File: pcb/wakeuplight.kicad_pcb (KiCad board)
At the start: 2 copper layers, 129 x 85 mm, 50 parts, among them J1 691322310002, J10 MKDS 3.5mm, J2 Conn_01x19, J3 Conn_01x19, J4 MAX98357A Breakout, J5 MKDS 3.5mm, J6 MKDS 3.5mm, J7 MPT 2,54, J8 MPT 2,54, J9 MKDS 3.5mm, Q1 PSMN1R2-30YLC, Q2 PSMN1R2-30YLC, Q3 T2N7002BK, U1 MCP14A0302, U2 MCP14A0302, U3 LMR16006YQ

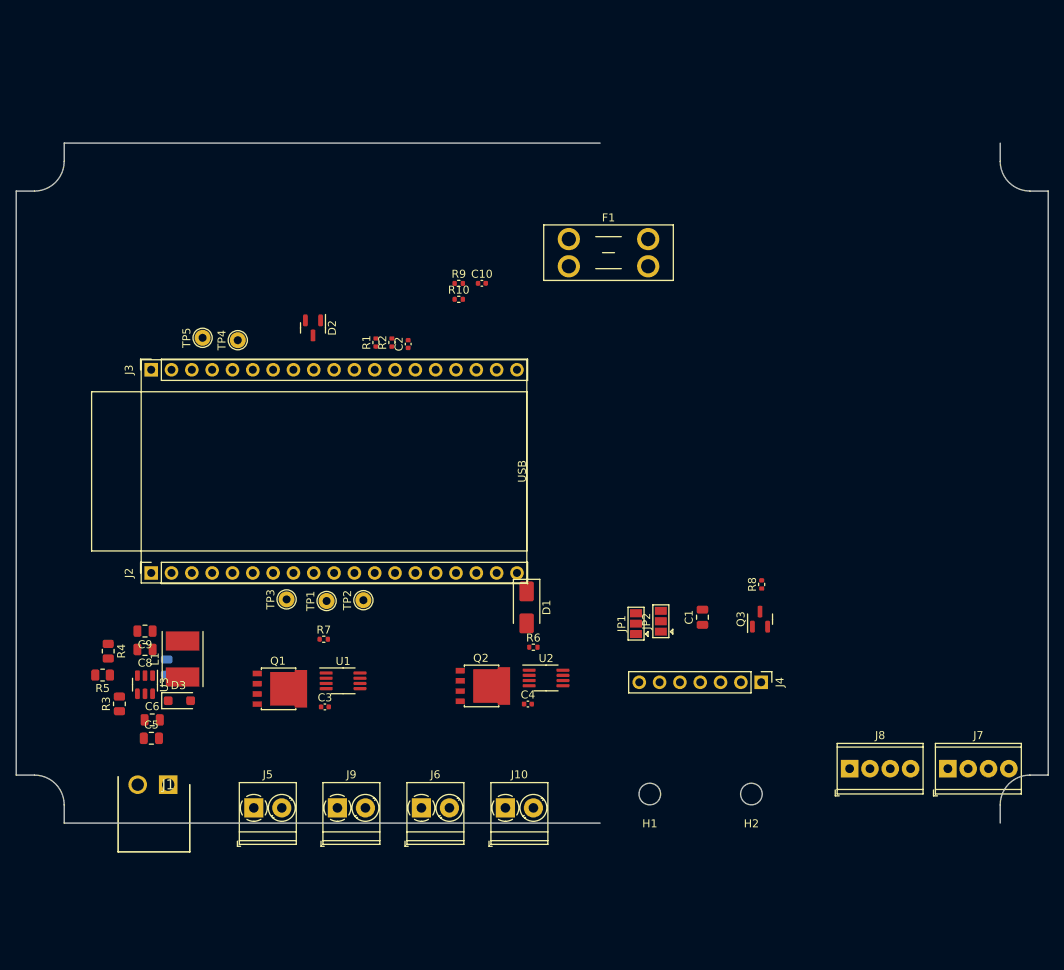
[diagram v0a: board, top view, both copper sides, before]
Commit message: work on PCB: line out + power done ; removed amplifier from board
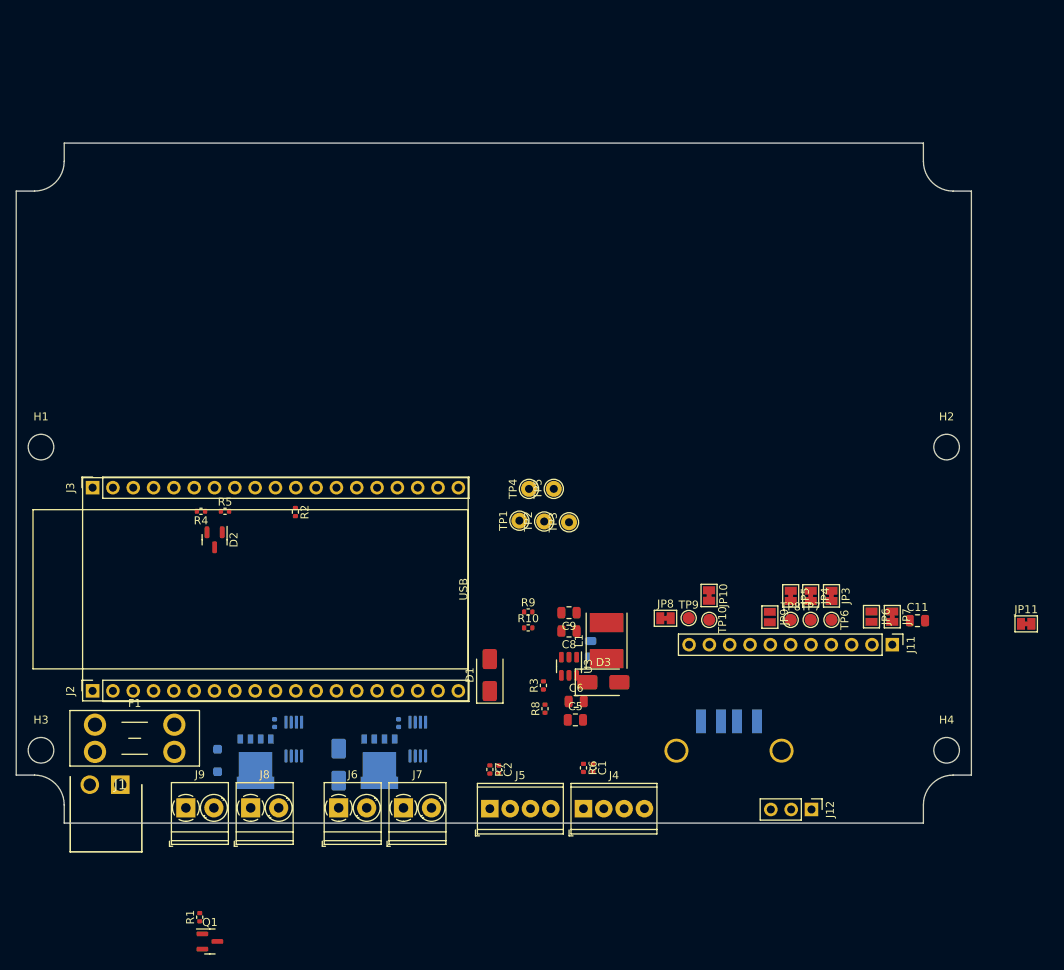
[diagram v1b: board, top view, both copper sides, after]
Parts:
- removed C10: 1uF 10V, Capacitor_SMD:C_0402_1005Metric
- removed J10: MKDS 3.5mm, TerminalBlock_Phoenix:TerminalBlock_Phoenix_PT-1,5-2-3.5-H_1x02_P3.50mm_Horizontal
- removed JP1, JP2: SolderJumper_3_Open, Jumper:SolderJumper-3_P1.3mm_Open_Pad1.0x1.5mm
- added C11: 10uF 10V, Capacitor_SMD:C_0805_2012Metric, F.Cu at (112.7, 59.7)
- added D4: SS16_R2_00001 1A, 42V, Diode_SMD:D_SMA, B.Cu at (40.3, 77.7)
- added D5: PMEG2020EH, Diode_SMD:D_SOD-123F, B.Cu at (25.2, 77.2)
- added H3: MountingHole, MountingHole:MountingHole_3.2mm_M3_DIN965, F.Cu at (3.10, 75.9)
- added H4: MountingHole, MountingHole:MountingHole_3.2mm_M3_DIN965, F.Cu at (116.3, 75.9)
- added J11: PCM5102A Breakout, Connector_PinHeader_2.54mm:PinHeader_1x11_P2.54mm_Vertical, F.Cu at (109.5, 62.7)
- added J12: Conn_01x03_Pin, Connector_PinHeader_2.54mm:PinHeader_1x03_P2.54mm_Vertical, F.Cu at (99.4, 83.3)
- added J13: USB_A, Connector_USB:USB_A_TE_292303-7_Horizontal, B.Cu at (89.1, 78.7)
- added JP10: SolderJumper_2_Bridged, Jumper:SolderJumper-2_P1.3mm_Bridged_Pad1.0x1.5mm, F.Cu at (86.6, 56.5)
- added JP11: SolderJumper_2_Bridged, Jumper:SolderJumper-2_P1.3mm_Bridged_Pad1.0x1.5mm, F.Cu at (126.2, 60.1)
- added JP3: SolderJumper_2_Bridged, Jumper:SolderJumper-2_P1.3mm_Bridged_Pad1.0x1.5mm, F.Cu at (101.9, 56.6)
- added JP4: SolderJumper_2_Bridged, Jumper:SolderJumper-2_P1.3mm_Bridged_Pad1.0x1.5mm, F.Cu at (99.3, 56.6)
- added JP5: SolderJumper_2_Bridged, Jumper:SolderJumper-2_P1.3mm_Bridged_Pad1.0x1.5mm, F.Cu at (96.8, 56.6)
- added JP6: SolderJumper_2_Open, Jumper:SolderJumper-2_P1.3mm_Open_Pad1.0x1.5mm, F.Cu at (106.9, 59.2)
- added JP7: SolderJumper_2_Bridged, Jumper:SolderJumper-2_P1.3mm_Bridged_Pad1.0x1.5mm, F.Cu at (109.5, 59.2)
- added JP8: SolderJumper_2_Bridged, Jumper:SolderJumper-2_P1.3mm_Bridged_Pad1.0x1.5mm, F.Cu at (81.2, 59.4)
- added JP9: SolderJumper_2_Open, Jumper:SolderJumper-2_P1.3mm_Open_Pad1.0x1.5mm, F.Cu at (94.2, 59.2)
- added TP10: TestPoint, TestPoint:TestPoint_Pad_D1.5mm, F.Cu at (86.6, 59.6)
- added TP6: TestPoint, TestPoint:TestPoint_Pad_D1.5mm, F.Cu at (101.9, 59.6)
- added TP7: TestPoint, TestPoint:TestPoint_Pad_D1.5mm, F.Cu at (99.3, 59.6)
- added TP8: TestPoint, TestPoint:TestPoint_Pad_D1.5mm, F.Cu at (96.8, 59.6)
- added TP9: TestPoint, TestPoint:TestPoint_Pad_D1.5mm, F.Cu at (84.1, 59.4)
- C1: value 10uF 10V -> 1uF 10V; footprint Capacitor_SMD:C_0805_2012Metric -> Capacitor_SMD:C_0402_1005Metric
- C3, C4, Q2, U1, U2: moved to B.Cu
- D3: value PMEG2020EH -> SS16_R2_00001 1A, 42V; footprint Diode_SMD:D_SOD-123F -> Diode_SMD:D_SMA
- H1, H2: footprint MountingHole:MountingHole_2.7mm_M2.5 -> MountingHole:MountingHole_3.2mm_M3_DIN965
- J4: value MAX98357A Breakout -> MPT 2,54; footprint Connector_PinHeader_2.54mm:PinHeader_1x07_P2.54mm_Vertical -> TerminalBlock_Phoenix:TerminalBlock_Phoenix_MPT-0,5-4-2.54_1x04_P2.54mm_Horizontal
- J5: value MKDS 3.5mm -> MPT 2,54; footprint TerminalBlock_Phoenix:TerminalBlock_Phoenix_PT-1,5-2-3.5-H_1x02_P3.50mm_Horizontal -> TerminalBlock_Phoenix:TerminalBlock_Phoenix_MPT-0,5-4-2.54_1x04_P2.54mm_Horizontal
- J7, J8: value MPT 2,54 -> MKDS 3.5mm; footprint TerminalBlock_Phoenix:TerminalBlock_Phoenix_MPT-0,5-4-2.54_1x04_P2.54mm_Horizontal -> TerminalBlock_Phoenix:TerminalBlock_Phoenix_PT-1,5-2-3.5-H_1x02_P3.50mm_Horizontal
- Q1: value PSMN1R2-30YLC -> T2N7002BK; footprint Package_TO_SOT_SMD:LFPAK56 -> Package_TO_SOT_SMD:SOT-23
- Q3: value T2N7002BK -> PSMN1R2-30YLC; footprint Package_TO_SOT_SMD:SOT-23 -> Package_TO_SOT_SMD:LFPAK56; moved to B.Cu
- R1: value 100k -> 1k
- R10: value 1k -> 10k
- R2, R8: value 1k -> 100k
- R3, R5: footprint Resistor_SMD:R_0805_2012Metric -> Resistor_SMD:R_0402_1005Metric
- R4: value 54k9 -> 10k; footprint Resistor_SMD:R_0805_2012Metric -> Resistor_SMD:R_0402_1005Metric
- R6, R7: value 10k -> 1k
- R9: value 100k -> 54k9
- moved H1 87.6 mm to (3.10, 38.0), turned to 0 degrees
- moved F1 84.8 mm to (9.85, 72.7)
- moved R1 75.1 mm to (22.9, 96.8)
- moved J8 75.0 mm to (29.3, 83.1)
- moved J7 68.2 mm to (48.4, 83.1)
- moved Q3 65.5 mm to (29.9, 77.2), turned to -90 degrees
- moved C2 54.4 mm to (60.3, 78.3), turned to -90 degrees
- moved C5 53.0 mm to (69.9, 72.1)
- moved D3 53.0 mm to (73.4, 67.4)
- moved R3 53.0 mm to (65.9, 67.8)
- moved C6 53.0 mm to (70.0, 69.8)
- moved C7 53.0 mm to (71.8, 63.2)
- moved L1 53.0 mm to (73.8, 62.2)
- moved C8 53.0 mm to (69.1, 61.0)
- moved C9 53.0 mm to (69.1, 58.7)
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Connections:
- C1 pad 1: +5V -> /button_1
- C2 pad 1: /button_1 -> /button_2
- C7 pad 2: Net-(D3-K) -> Net-(D5-K)
- D3 pad 1: Net-(D3-K) -> +24V
- D3 pad 2: GND -> Net-(D3-A)
- J4 pad 1: /I2S_WS -> Net-(J4-Pin_1)
- J4 pad 2: /I2S_BCLK -> GND
- J4 pad 3: /I2S_DOUT -> Net-(J4-Pin_1)
- J4 pad 4: /gain -> GND
- J5 pad 1: +24V -> Net-(J5-Pin_1)
- J5 pad 2: Net-(J5-Pin_2) -> GND
- J6 pad 2: Net-(J10-Pin_2) -> Net-(D3-A)
- J7 pad 1: Net-(J7-Pin_1) -> +24V
- J7 pad 2: GND -> Net-(D3-A)
- J8 pad 1: Net-(J8-Pin_1) -> +24V
- J8 pad 2: GND -> Net-(D4-A)
- J9 pad 2: Net-(J5-Pin_2) -> Net-(D4-A)
- L1 pad 1: Net-(D3-K) -> Net-(D5-K)
- Q1 pad 1: GND -> Net-(Q1-G)
- Q1 pad 2: GND -> unconnected-(Q1-S-Pad2)
- Q2 pad 5: Net-(J10-Pin_2) -> Net-(D3-A)
- Q3 pad 1: Net-(Q3-G) -> GND
- Q3 pad 2: /sd_mode -> GND
- R1 pad 1: /button_1 -> Net-(Q1-G)
- R1 pad 2: +3V3 -> /~{EN}_audio
- R10 pad 1: /button_2 -> Net-(U3-FB)
- R10 pad 2: Net-(J8-Pin_1) -> GND
- R2 pad 2: Net-(J7-Pin_1) -> +3V3
- R3 pad 1: +24V -> /button_2
- R3 pad 2: Net-(U3-~{SHDN}) -> +3V3
- R4 pad 1: +5V -> GND
- R4 pad 2: Net-(U3-FB) -> /EN_top
- R5 pad 1: Net-(U3-FB) -> GND
- R5 pad 2: GND -> /EN_bottom
- R6 pad 1: GND -> /button_1
- R6 pad 2: /EN_bottom -> Net-(J4-Pin_1)
- R7 pad 1: GND -> /button_2
- R7 pad 2: /EN_top -> Net-(J5-Pin_1)
- R8 pad 1: Net-(Q3-G) -> +24V
- R8 pad 2: /~{EN}_audio -> Net-(U3-~{SHDN})
- R9 pad 1: /button_2 -> +5V
- R9 pad 2: +3V3 -> Net-(U3-FB)
- TP1 pad 1: Net-(J2-Pin_9) -> Net-(J2-Pin_8)
- TP2 pad 1: Net-(J2-Pin_10) -> Net-(J2-Pin_9)
- TP3 pad 1: Net-(J2-Pin_8) -> Net-(J2-Pin_10)
- TP4 pad 1: Net-(J3-Pin_3) -> Net-(J3-Pin_2)
- TP5 pad 1: Net-(J3-Pin_2) -> Net-(J3-Pin_3)
- U1 pad 6: Net-(Q1-G) -> Net-(Q2-G)
- U1 pad 7: Net-(Q1-G) -> Net-(Q2-G)
- U2 pad 6: Net-(Q2-G) -> Net-(Q3-G)
- U2 pad 7: Net-(Q2-G) -> Net-(Q3-G)
- U3 pad 6: Net-(D3-K) -> Net-(D5-K)
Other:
- board size 129 x 85 mm -> 119.4 x 85 mm

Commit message: PCB done
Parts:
- added C12: 1uF 35V, Capacitor_SMD:C_0805_2012Metric, F.Cu at (73.3, 32.2)
- added C13: 1uF 35V, Capacitor_SMD:C_0805_2012Metric, F.Cu at (73.3, 34.4)
- added C14: 100nF 50V, Capacitor_SMD:C_0805_2012Metric, B.Cu at (72.8, 28.9)
- added C15: 10uF 10V, Capacitor_SMD:C_0805_2012Metric, F.Cu at (72.3, 25.4)
- added C16: 10uF 10V, Capacitor_SMD:C_0805_2012Metric, F.Cu at (72.3, 23.2)
- added D6: PMEG2020EH, Diode_SMD:D_SOD-123F, F.Cu at (76.8, 33.3)
- added H7: MountingHole, MountingHole:MountingHole_3.2mm_M3_DIN965, F.Cu at (61.0, 14.4)
- added JP12: SolderJumper_2_Open, Jumper:SolderJumper-2_P1.3mm_Open_Pad1.0x1.5mm, F.Cu at (84.0, 13.9)
- added L2: 22uH SRN5040-220M, Inductor_SMD:L_Taiyo-Yuden_NR-50xx_HandSoldering, F.Cu at (77.0, 27.2)
- added R11: 200k, Resistor_SMD:R_0402_1005Metric, F.Cu at (69.5, 31.3)
- added R12: 54k9, Resistor_SMD:R_0402_1005Metric, F.Cu at (69.8, 26.3)
- added R13: 10k, Resistor_SMD:R_0402_1005Metric, F.Cu at (69.8, 28.4)
- added U4: LMR16006YQ, Package_TO_SOT_SMD:SOT-23-6, F.Cu at (72.2, 28.9)
- D3, JP11: moved to B.Cu
- D5: moved to F.Cu
- J11: footprint Connector_PinHeader_2.54mm:PinHeader_1x11_P2.54mm_Vertical -> Connector_PinSocket_2.54mm:PinSocket_1x11_P2.54mm_Vertical
- J12: footprint Connector_PinHeader_2.54mm:PinHeader_1x03_P2.54mm_Vertical -> Connector_PinSocket_2.54mm:PinSocket_1x03_P2.54mm_Vertical
- R8: value 100k -> 200k
- moved Q1 78.8 mm to (37.0, 22.1), turned to 90 degrees
- moved R1 72.6 mm to (36.1, 25.4), turned to -90 degrees
- moved R3 68.0 mm to (35.6, 6.90), turned to -90 degrees
- moved H1 67.5 mm to (61.0, 3.30)
- moved TP5 64.4 mm to (13.6, 7.60)
- moved TP4 64.4 mm to (10.5, 7.60)
- moved D5 58.9 mm to (64.7, 33.5)
- moved JP11 53.5 mm to (82.2, 29.7)
- moved JP6 50.5 mm to (80.5, 16.1)
- moved D1 46.6 mm to (58.9, 19.9), turned to 0 degrees
- moved D3 44.3 mm to (40.6, 37.6), turned to 90 degrees
- moved TP3 44.0 mm to (31.8, 24.1)
- moved TP2 43.9 mm to (28.7, 24.1)
- moved TP1 43.9 mm to (25.6, 24.1)
- moved D4 43.1 mm to (25.2, 37.3), turned to -90 degrees
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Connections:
- net /~{EN}_audio renamed /EN_audio
- net Net-(U3-~{SHDN}) renamed /regulator_5v/~{SHDN}
- J13 pad 1: +5V -> /5V_audio
- J2 pad 3: unconnected-(J2-Pin_3-Pad3) -> GND
- J2 pad 4: unconnected-(J2-Pin_4-Pad4) -> GND
- J2 pad 5: unconnected-(J2-Pin_5-Pad5) -> GND
- J2 pad 6: unconnected-(J2-Pin_6-Pad6) -> GND
- J2 pad 7: unconnected-(J2-Pin_7-Pad7) -> GND
- J3 pad 15: unconnected-(J3-Pin_15-Pad15) -> /mute
- J3 pad 6: /EN_top -> /EN_bottom
- J3 pad 8: /EN_bottom -> /EN_top
- Q1 pad 2: unconnected-(Q1-S-Pad2) -> /regulator_5v_audio/~{SHDN}
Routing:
- net +5V: track 0.00 -> 103.6 mm, vias 0 -> 5
- net +3V3: track 0.00 -> 95.5 mm, vias 0 -> 3
- net /I2S_DOUT: track 0.00 -> 81.6 mm, vias 0 -> 2
- net /I2S_WS: track 0.00 -> 79.3 mm, vias 0 -> 2
- net /button_1: track 0.00 -> 72.2 mm, vias 0 -> 4
- net /I2S_BCLK: track 0.00 -> 70.8 mm, vias 0 -> 1
- net /button_2: track 0.00 -> 57.7 mm, vias 0 -> 4
- net /EN_top: track 0.00 -> 55.1 mm, vias 0 -> 3
- net /mute: track 0.00 -> 48.7 mm, vias 0 -> 3
- net /EN_bottom: track 0.00 -> 42.2 mm, vias 0 -> 3
- net /regulator_5v_audio/~{SHDN}: track 0.00 -> 42.1 mm, vias 0 -> 2
- net /PCM5102A/PCM_3V3: track 0.00 -> 35.9 mm, vias 0 -> 2
- net +24V: track 0.00 -> 34.6 mm
- net /5V_audio: track 0.00 -> 26.8 mm, vias 0 -> 6
- net /PWM_sig: track 0.00 -> 22.5 mm
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- added copper zone on F.Cu, net +24V
- added copper zone on F.Cu, net +5V
- added copper zone on F.Cu, net /5V_audio
- added copper zone on B.Cu, net GND
- added copper zone on F.Cu, net GND
- added copper zone on B.Cu, net Net-(D3-A)
- added copper zone on B.Cu, net Net-(D4-A)
- added copper zone on F.Cu, net Net-(D5-K)
- added copper zone on F.Cu, net Net-(D6-K)
- added copper zone on F.Cu, net Net-(J1-Pin_2)
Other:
- board size 119.4 x 85 mm -> 113.1 x 44.7 mm
- board text added: "DMP"
- board text added: "FLT"
- board text added: "FMT"
- board text added: "SCL"
- board text added: "Wakeuplight v2 by Solderdev 202402"
- board text added: "XMT"

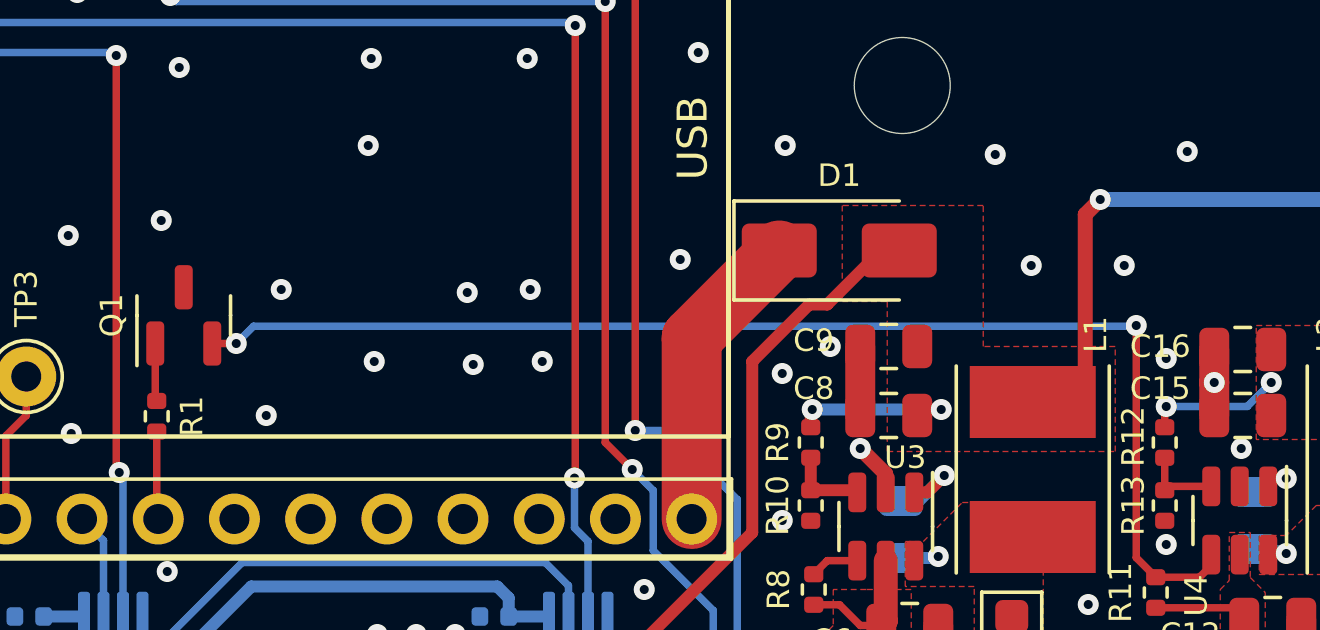
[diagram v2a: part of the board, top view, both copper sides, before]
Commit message: PCB: renamed "EN_audio" to "~EN_audio" ; added input capacitor (PSU noise) ; fixed mirrored MOSFET
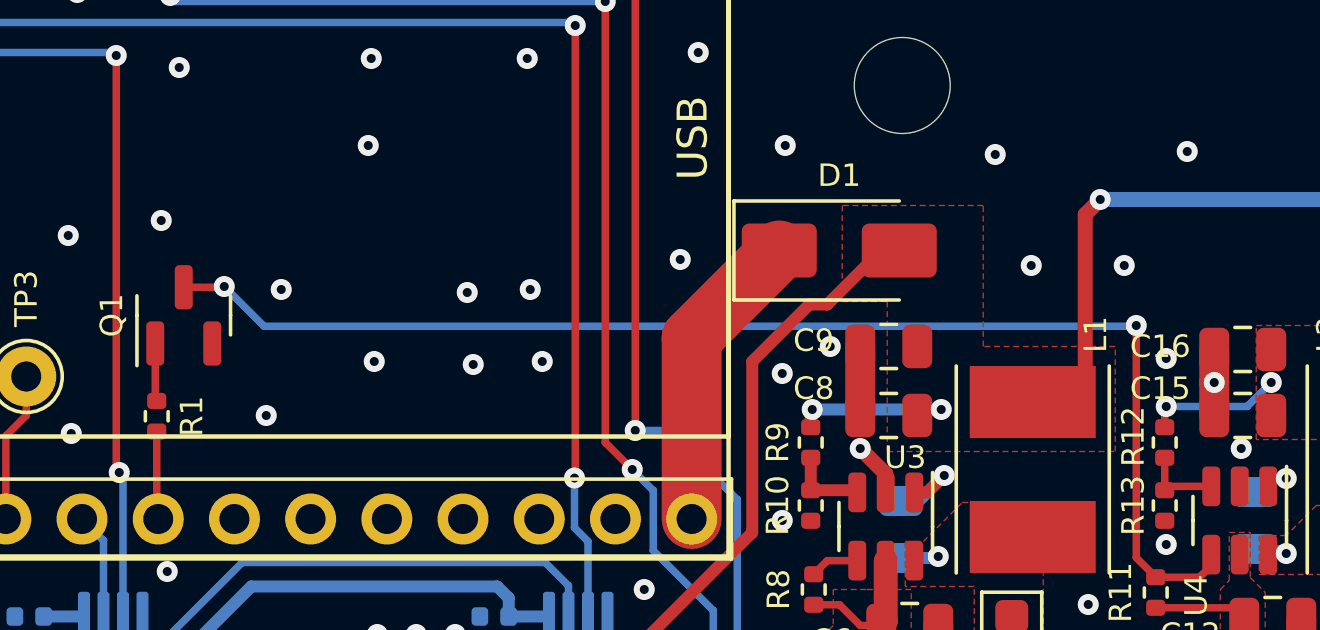
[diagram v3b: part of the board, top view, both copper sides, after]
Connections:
- net /EN_audio renamed /~{EN}_audio
- Q1 pad 2: /regulator_5v_audio/~{SHDN} -> GND
- Q1 pad 3: GND -> /regulator_5v_audio/~{SHDN}
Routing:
- net /regulator_5v_audio/~{SHDN}: track 42.1 -> 43.4 mm
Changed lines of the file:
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@@
   (net 58 "unconnected-(J13-D+-Pad3)")
   (net 59 "Net-(J13-Shield)")
-  (net 60 "/EN_audio")
+  (net 60 "/~{EN}_audio")
   (net 61 "/regulator_5v_audio/~{SHDN}")
   (net 62 "/regulator_5v/~{SHDN}")
@@
       (net 35 "Net-(Q1-G)") (pintype "passive"))
     (pad "2" smd roundrect (at 0.51 0 270) (size 0.54 0.64) (layers "F.Cu" "F.Paste" "F.Mask") (roundrect_rratio 0.25)
-      (net 60 "/EN_audio") (pintype "passive"))
+      (net 60 "/~{EN}_audio") (pintype "passive"))
     (model "${KICAD6_3DMODEL_DIR}/Resistor_SMD.3dshapes/R_0402_1005Metric.wrl"
       (offset (xyz 0 0 0))
@@
       (net 35 "Net-(Q1-G)") (pinfunction "G") (pintype "input"))
     (pad "2" smd roundrect (at -0.9375 0.95 90) (size 1.475 0.6) (layers "F.Cu" "F.Paste" "F.Mask") (roundrect_rratio 0.25)
-      (net 61 "/regulator_5v_audio/~{SHDN}") (pinfunction "S") (pintype "passive"))
+      (net 2 "GND") (pinfunction "S") (pintype "passive"))
     (pad "3" smd roundrect (at 0.9375 0 90) (size 1.475 0.6) (layers "F.Cu" "F.Paste" "F.Mask") (roundrect_rratio 0.25)
-      (net 2 "GND") (pinfunction "D") (pintype "passive"))
+      (net 61 "/regulator_5v_audio/~{SHDN}") (pinfunction "D") (pintype "passive"))
     (model "${KICAD6_3DMODEL_DIR}/Package_TO_SOT_SMD.3dshapes/SOT-23.wrl"
       (offset (xyz 0 0 0))
@@
       (net 14 "/PWM_sig") (pinfunction "Pin_11") (pintype "passive"))
     (pad "12" thru_hole oval (at 0 27.94 90) (size 1.7 1.7) (drill 1) (layers "*.Cu" "*.Mask")
-      (net 60 "/EN_audio") (pinfunction "Pin_12") (pintype "passive"))
+      (net 60 "/~{EN}_audio") (pinfunction "Pin_12") (pintype "passive"))
     (pad "13" thru_hole oval (at 0 30.48 90) (size 1.7 1.7) (drill 1) (layers "*.Cu" "*.Mask")
       (net 16 "unconnected-(J2-Pin_13-Pad13)") (pinfunction "Pin_13") (pintype "passive+no_connect"))
@@
   (segment (start 71.3 30.4) (end 71.3 30.0375) (width 0.25) (layer "F.Cu") (net 61))
   (segment (start 68.8 30.14) (end 69.45 30.79) (width 0.25) (layer "F.Cu") (net 61))
-  (segment (start 38 23) (end 38.8 23) (width 0.25) (layer "F.Cu") (net 61))
   (segment (start 69.45 30.79) (end 70.91 30.79) (width 0.25) (layer "F.Cu") (net 61))
   (segment (start 70.91 30.79) (end 71.3 30.4) (width 0.25) (layer "F.Cu") (net 61))
   (segment (start 68.8 22.4) (end 68.8 30.14) (width 0.25) (layer "F.Cu") (net 61))
-  (via (at 38.8 23) (size 0.7) (drill 0.3) (layers "F.Cu" "B.Cu") (net 61))
+  (segment (start 37.05 21.125) (end 38.375 21.125) (width 0.25) (layer "F.Cu") (net 61))
+  (segment (start 38.375 21.125) (end 38.4 21.1) (width 0.25) (layer "F.Cu") (net 61))
+  (via (at 38.4 21.1) (size 0.7) (drill 0.3) (layers "F.Cu" "B.Cu") (net 61))
   (via (at 68.8 22.4) (size 0.7) (drill 0.3) (layers "F.Cu" "B.Cu") (net 61))
-  (segment (start 68.775 22.425) (end 39.375 22.425) (width 0.25) (layer "B.Cu") (net 61))
-  (segment (start 39.375 22.425) (end 38.8 23) (width 0.25) (layer "B.Cu") (net 61))
-  (segment (start 68.8 22.4) (end 68.775 22.425) (width 0.25) (layer "B.Cu") (net 61))
+  (segment (start 39.725 22.425) (end 68.775 22.425) (width 0.25) (layer "B.Cu") (net 61))
+  (segment (start 38.4 21.1) (end 39.725 22.425) (width 0.25) (layer "B.Cu") (net 61))
+  (segment (start 68.775 22.425) (end 68.8 22.4) (width 0.25) (layer "B.Cu") (net 61))
   (segment (start 58.5025 30.2375) (end 58.05 30.69) (width 0.25) (layer "F.Cu") (net 62))
   (segment (start 59.5 30.2375) (end 58.5025 30.2375) (width 0.25) (layer "F.Cu") (net 62))
